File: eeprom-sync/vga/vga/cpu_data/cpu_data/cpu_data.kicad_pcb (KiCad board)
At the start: 2 copper layers, 78 x 44.7 mm, 34 parts, among them J1 Conn_02x06_Odd_Even, J10 Conn_01x03_Female, J11 Conn_01x02_Female, J12 Conn_02x05_Odd_Even, J2 Conn_01x04_Male, J3 Conn_01x04_Female, J4 Conn_01x15_Female, J5 Conn_01x15_Female, J6 Conn_01x08_Female, J7 Conn_02x03_Odd_Even, J8 Conn_02x08_Odd_Even, J9 Conn_01x08_Female, Q1 Q_NMOS_GSD, U1 GAL22V10, U2 74HC14, U3 74LS02, U4 IDT7205L12JG, U5 74LS573

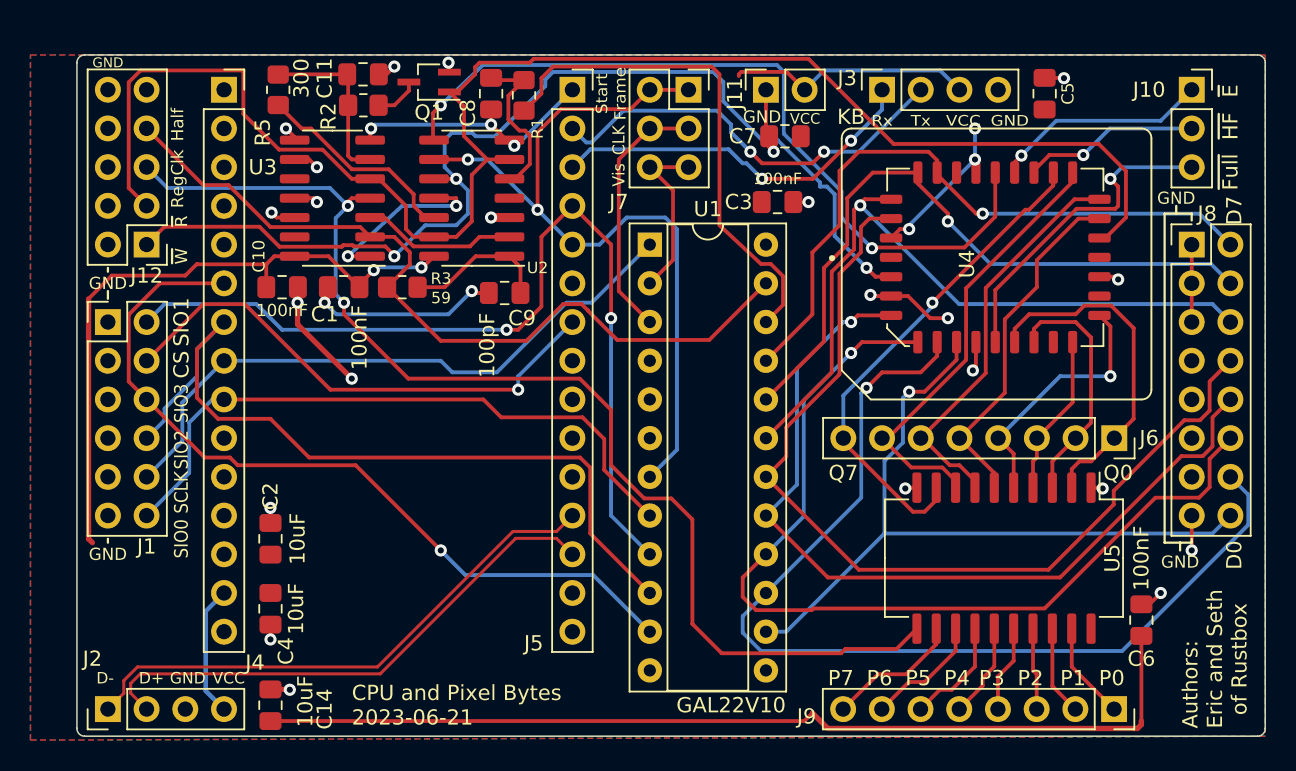
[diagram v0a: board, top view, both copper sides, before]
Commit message: added power and pixel indicator LEDs, rearranged and changed some headers for clearance of the GAL, fixed a location issue with a decoup cap
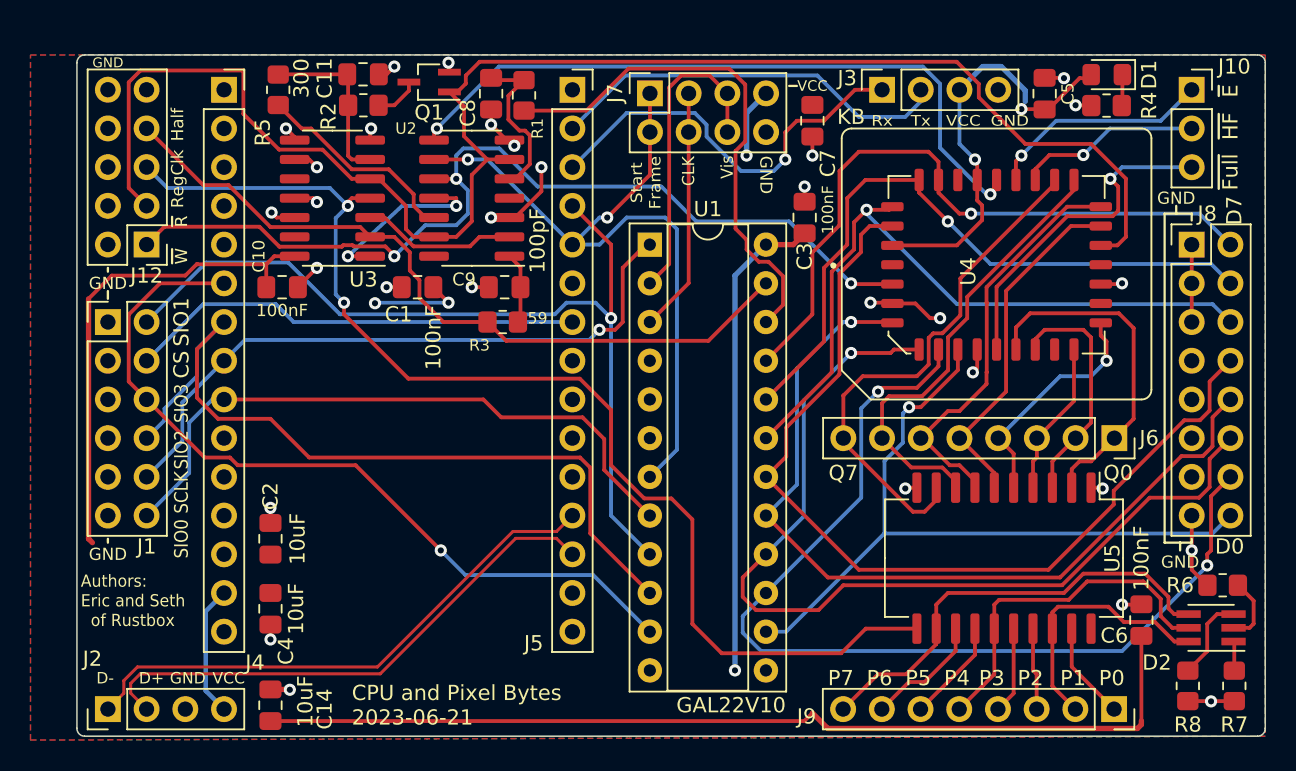
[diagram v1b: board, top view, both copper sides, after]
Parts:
- removed J11: Conn_01x02_Female, Connector_PinSocket_2.54mm:PinSocket_1x02_P2.54mm_Vertical
- added D1: LED, LED_SMD:LED_0805_2012Metric_Pad1.15x1.40mm_HandSolder, F.Cu at (146.8, 60.0)
- added D2: LED_RGB, LED_SMD:LED_Avago_PLCC6_3x2.8mm, F.Cu at (153.7, 96.3)
- added R4: R, Resistor_SMD:R_0805_2012Metric_Pad1.20x1.40mm_HandSolder, F.Cu at (146.8, 62.0)
- added R6: R, Resistor_SMD:R_0805_2012Metric_Pad1.20x1.40mm_HandSolder, F.Cu at (154.4, 93.5)
- added R7: R, Resistor_SMD:R_0805_2012Metric_Pad1.20x1.40mm_HandSolder, F.Cu at (155.2, 100.1)
- added R8: R, Resistor_SMD:R_0805_2012Metric_Pad1.20x1.40mm_HandSolder, F.Cu at (152.1, 100.1)
- J7: value Conn_02x03_Odd_Even -> Conn_02x04_Odd_Even; footprint Connector_PinSocket_2.54mm:PinSocket_2x03_P2.54mm_Vertical -> Connector_PinSocket_2.54mm:PinSocket_2x04_P2.54mm_Vertical
- R1: value R -> 34
- moved R3 6.97 mm to (107.2, 76.2)
- moved C1 4.85 mm to (101.6, 73.9)
- moved J7 2.54 mm to (116.8, 61.2), turned to 90 degrees
- moved C7 2.07 mm to (127.5, 63.0), turned to -90 degrees
- moved C3 2.05 mm to (127.0, 69.3), turned to -90 degrees
- moved C9 0.38 mm to (107.3, 73.9)
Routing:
- net VCC: track 142.5 -> 174.5 mm, vias 5 -> 6
- net GND: track 75.8 -> 53.1 mm, vias 28 -> 30
- net /P7: track 8.90 -> 29.4 mm
- net /P4: track 6.23 -> 23.1 mm
- net /P1: track 5.91 -> 17.0 mm
- net /Vis: track 11.4 -> 20.5 mm
- net /~{W}: track 70.2 -> 61.7 mm
- net /Reset: track 52.1 -> 45.9 mm
- net Net-(D2-Pad3): track 0.00 -> 5.59 mm
- net Net-(C9-Pad1): track 9.58 -> 4.68 mm
- net Net-(R6-Pad1): track 0.00 -> 4.39 mm
- net /CS: track 34.2 -> 30.0 mm, vias 1 -> 0
- net /Half: track 53.4 -> 49.4 mm
- net /StartFrame: track 52.4 -> 48.6 mm
- net /KB_{Rx}: track 24.8 -> 27.1 mm, vias 2 -> 1
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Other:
- board text added: "J7"

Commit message: gnd-ing the /OE on the gal
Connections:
- U1 pad 13: unconnected-(U1-Pad13) -> GND

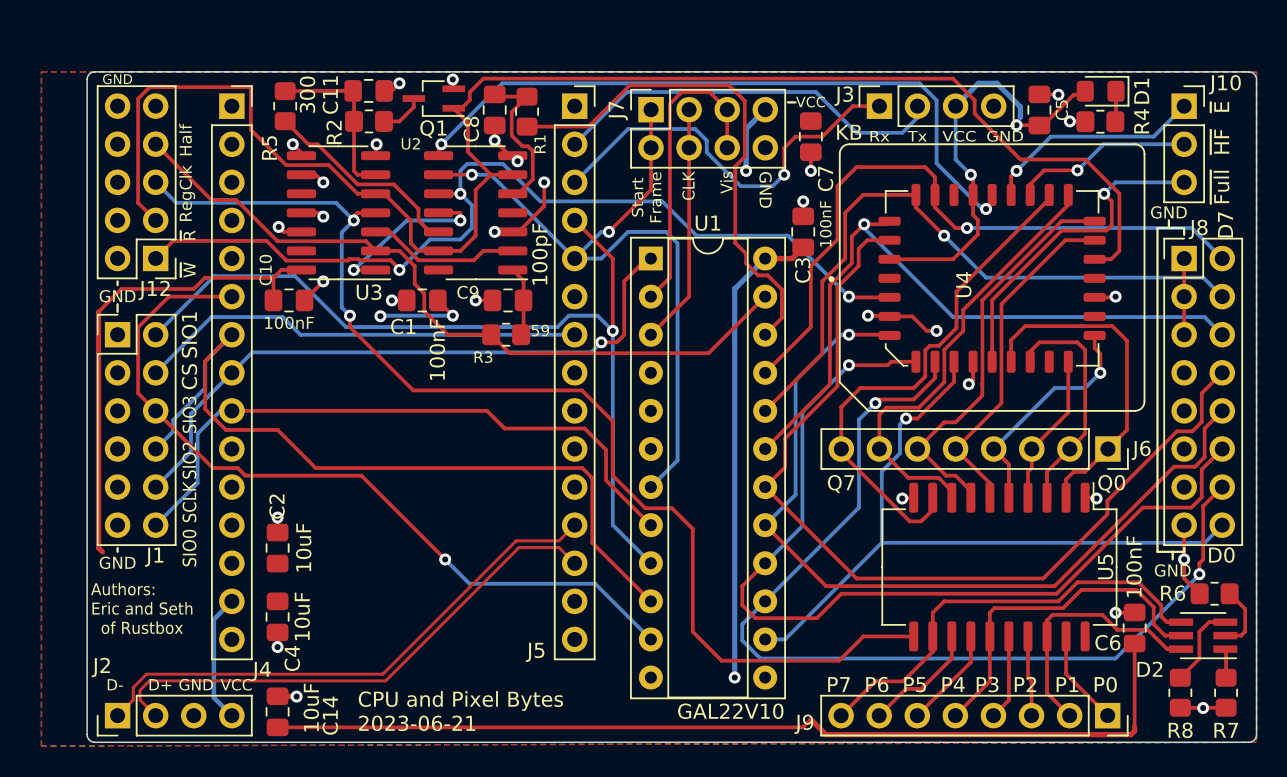
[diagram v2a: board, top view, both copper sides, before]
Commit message: updating board to use clocked latches as the data mile markers instead of RC time circuits. Also adding a clock board breadboardable circuit module
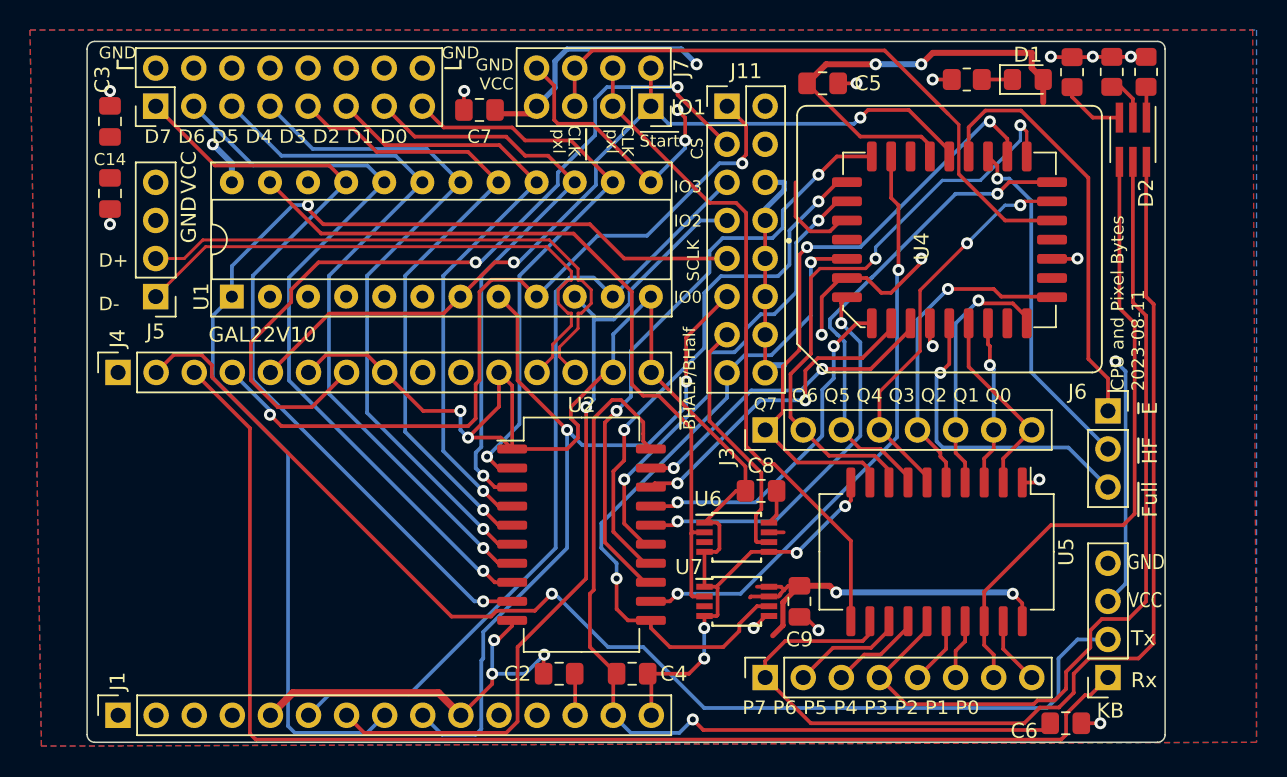
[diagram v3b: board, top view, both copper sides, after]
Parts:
- removed C1, C10: 100nF, Capacitor_SMD:C_0805_2012Metric_Pad1.18x1.45mm_HandSolder
- removed C11: 100pF, Capacitor_SMD:C_0805_2012Metric_Pad1.18x1.45mm_HandSolder
- removed J12: Conn_02x05_Odd_Even, Connector_PinHeader_2.54mm:PinHeader_2x05_P2.54mm_Vertical
- removed J9: Conn_01x08_Female, Connector_PinSocket_2.54mm:PinSocket_1x08_P2.54mm_Vertical
- removed Q1: Q_NMOS_GSD, Package_TO_SOT_SMD:SOT-323_SC-70_Handsoldering
- removed R1: 34, Resistor_SMD:R_0805_2012Metric_Pad1.20x1.40mm_HandSolder
- removed R2: 50, Resistor_SMD:R_0805_2012Metric_Pad1.20x1.40mm_HandSolder
- removed R3: 59, Resistor_SMD:R_0805_2012Metric_Pad1.20x1.40mm_HandSolder
- removed R5: 300, Resistor_SMD:R_0805_2012Metric_Pad1.20x1.40mm_HandSolder
- removed U3: 74LS02, Package_SO:SOIC-14_3.9x8.7mm_P1.27mm
- added J11: Conn_02x08_Odd_Even, Connector_PinHeader_2.54mm:PinHeader_2x08_P2.54mm_Vertical, F.Cu at (121.9, 61.0)
- added U6: 74AUC2G125, Package_SO:TSSOP-8_3x3mm_P0.65mm, F.Cu at (122.6, 89.7)
- added U7: 74LVC2G240, Package_SO:TSSOP-8_3x3mm_P0.65mm, F.Cu at (122.6, 94.0)
- C8, C9: value 100pF -> 100nF
- J1: value Conn_02x06_Odd_Even -> Conn_01x15_Socket; footprint Connector_PinHeader_2.54mm:PinHeader_2x06_P2.54mm_Vertical -> Connector_PinSocket_2.54mm:PinSocket_1x15_P2.54mm_Vertical
- J10: value Conn_01x03_Female -> Conn_01x08_Socket; footprint Connector_PinSocket_2.54mm:PinSocket_1x03_P2.54mm_Vertical -> Connector_PinSocket_2.54mm:PinSocket_1x08_P2.54mm_Vertical
- J2: value Conn_01x04_Male -> Conn_01x04_Socket; footprint Connector_PinHeader_2.54mm:PinHeader_1x04_P2.54mm_Vertical -> Connector_PinSocket_2.54mm:PinSocket_1x04_P2.54mm_Vertical
- J3: value Conn_01x04_Female -> Conn_01x08_Socket; footprint Connector_PinSocket_2.54mm:PinSocket_1x04_P2.54mm_Vertical -> Connector_PinHeader_2.54mm:PinHeader_1x08_P2.54mm_Vertical
- J4: value Conn_01x15_Female -> Conn_01x15_Socket
- J5: value Conn_01x15_Female -> Conn_01x04_Pin; footprint Connector_PinSocket_2.54mm:PinSocket_1x15_P2.54mm_Vertical -> Connector_PinHeader_2.54mm:PinHeader_1x04_P2.54mm_Vertical
- J6: value Conn_01x08_Female -> Conn_01x03_Socket; footprint Connector_PinSocket_2.54mm:PinSocket_1x08_P2.54mm_Vertical -> Connector_PinSocket_2.54mm:PinSocket_1x03_P2.54mm_Vertical
- U2: value 74HC14 -> 74LS573; footprint Package_SO:SOIC-14_3.9x8.7mm_P1.27mm -> Package_SO:SOIC-20W_7.5x15.4mm_P1.27mm
- moved J8 69.3 mm to (83.8, 61.0), turned to 90 degrees
- moved J2 66.1 mm to (147.3, 99.1), turned to 180 degrees
- moved J10 47.2 mm to (124.5, 99.1), turned to 90 degrees
- moved C3 46.8 mm to (80.8, 62.0)
- moved R7 42.6 mm to (144.9, 58.7), turned to 90 degrees
- moved R8 41.5 mm to (149.9, 58.7), turned to 90 degrees
- moved C14 36.3 mm to (80.8, 66.8), turned to 90 degrees
- moved R6 35.5 mm to (147.6, 58.7), turned to 90 degrees
- moved D2 33.4 mm to (149.0, 63.2), turned to -90 degrees
- moved C8 31.0 mm to (124.2, 86.6), turned to 0 degrees
- moved J5 30.7 mm to (83.8, 73.7), turned to 180 degrees
- moved U1 28.1 mm to (88.9, 73.7), turned to 90 degrees
- moved C9 27.9 mm to (126.7, 94.0), turned to 90 degrees
- moved J1 25.4 mm to (81.3, 101.6), turned to 90 degrees
- moved C4 23.9 mm to (115.6, 98.8), turned to 180 degrees
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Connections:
- C8 pad 1: Net-(C8-Pad1) -> GND
- C8 pad 2: GND -> VCC
- C9 pad 1: Net-(C9-Pad1) -> GND
- C9 pad 2: GND -> VCC
- D2 pad 1: Net-(D2-Pad1) -> Net-(D2-RK)
- D2 pad 3: Net-(D2-Pad3) -> Net-(D2-BK)
- D2 pad 4: /P7 -> /P1
- D2 pad 6: /P1 -> /P7
- J1 pad 10: /SCLK -> GND
- J1 pad 11: GND -> unconnected-(J1-Pin_11-Pad11)
- J1 pad 12: /SIO0 -> unconnected-(J1-Pin_12-Pad12)
- J1 pad 2: /SIO1 -> unconnected-(J1-Pin_2-Pad2)
- J1 pad 3: GND -> unconnected-(J1-Pin_3-Pad3)
- J1 pad 4: /CS -> unconnected-(J1-Pin_4-Pad4)
- J1 pad 7: GND -> /SIO2
- J1 pad 8: /SIO2 -> /SCLK
- J1 pad 9: GND -> /SIO0
- J10 pad 1: /Empty -> /P7
- J10 pad 2: /HalfFull -> /P6
- J10 pad 3: /Full -> /P5
- J2 pad 1: /D- -> /KB_{Rx}
- J2 pad 2: /D+ -> /KB_{Tx}
- J2 pad 3: GND -> VCC
- J2 pad 4: VCC -> GND
- J3 pad 1: /KB_{Rx} -> /Q7
- J3 pad 2: /KB_{Tx} -> /Q6
- J3 pad 3: VCC -> /Q5
- J3 pad 4: GND -> /Q4
- J4 pad 10: GND -> unconnected-(J4-Pin_10-Pad10)
- J4 pad 11: unconnected-(J4-Pad11) -> GND
- J4 pad 12: unconnected-(J4-Pad12) -> /D-
- J4 pad 13: VCC -> /D+
- J4 pad 14: VCC -> GND
- J4 pad 2: unconnected-(J4-Pad2) -> /KB_{Tx}
- J4 pad 3: unconnected-(J4-Pad3) -> /KB_{Rx}
- J4 pad 4: unconnected-(J4-Pad4) -> /SIO1
- J4 pad 5: GND -> /~{StartFrame}
- J4 pad 6: /SIO3 -> GND
- J4 pad 7: /SIO2 -> /CS
- J4 pad 8: /SCLK -> GND
- J4 pad 9: /SIO0 -> unconnected-(J4-Pin_9-Pad9)
- J5 pad 1: GND -> /D-
- J5 pad 2: /KB_{Tx} -> /D+
- J5 pad 3: /KB_{Rx} -> GND
- J5 pad 4: /SIO1 -> VCC
- J6 pad 1: /Q0 -> /Empty
- J6 pad 2: /Q1 -> /HalfFull
- J6 pad 3: /Q2 -> /Full
- J7 pad 1: /StartFrame -> /~{StartFrame}
- J7 pad 2: /StartFrame -> /~{StartFrame}
- J7 pad 3: /CLK -> /CLK_{pixel}
- J7 pad 4: /CLK -> /CLK_{pixel}
- J7 pad 5: /Vis -> /~{CLK_{pixel}}
- J7 pad 6: /Vis -> /~{CLK_{pixel}}
- J8 pad 1: GND -> /D7
- J8 pad 10: /D3 -> GND
- J8 pad 11: GND -> /D2
- J8 pad 12: /D2 -> GND
- J8 pad 13: GND -> /D1
- J8 pad 14: /D1 -> GND
- J8 pad 15: GND -> /D0
- J8 pad 16: /D0 -> GND
- J8 pad 2: /D7 -> GND
- J8 pad 3: GND -> /D6
- J8 pad 4: /D6 -> GND
- J8 pad 5: GND -> /D5
- J8 pad 6: /D5 -> GND
- J8 pad 7: GND -> /D4
- J8 pad 8: /D4 -> GND
- J8 pad 9: GND -> /D3
- R7 pad 1: Net-(D2-Pad1) -> Net-(D2-BK)
- R8 pad 1: Net-(D2-Pad3) -> Net-(D2-RK)
- U1 pad 2: /Vis -> unconnected-(U1-I2-Pad2)
- U1 pad 22: /CLK_{pixel} -> unconnected-(U1-IO2-Pad22)
- U1 pad 3: /CLK -> unconnected-(U1-I3-Pad3)
- U1 pad 7: /StartFrame -> /~{StartFrame}
- U2 pad 1: Net-(C9-Pad1) -> GND
- U2 pad 10: /~{W} -> GND
- U2 pad 11: Net-(U2-Pad11) -> /~{BHalf}
- U2 pad 12: Net-(R5-Pad2) -> /L7
- U2 pad 13: /~{R} -> /L6
- U2 pad 14: VCC -> /L5
- U2 pad 2: Net-(U2-Pad2) -> /D0
- U2 pad 3: GND -> /D1
- U2 pad 4: unconnected-(U2-Pad4) -> /D2
- U2 pad 5: Net-(C8-Pad1) -> /D3
- U2 pad 6: /~{R} -> /D4
- U2 pad 7: GND -> /D5
- U2 pad 8: /Reset -> /D6
- U2 pad 9: /StartFrame -> /D7
- U4 pad 18: /~{R} -> /~{CLK_{pixel}}
- U4 pad 2: /~{W} -> /~{BHalf}
- U4 pad 25: /Reset -> /~{StartFrame}
- U4 pad 28: /D7 -> /L7
- U4 pad 29: /D6 -> /L6
- U4 pad 30: /D5 -> /L5
- U4 pad 31: /D4 -> /L4
- U4 pad 4: /D3 -> /L3
- U4 pad 5: /D2 -> /L2
- U4 pad 6: /D1 -> /L1
- U4 pad 7: /D0 -> /L0
- U5 pad 11: /RegClk -> /CLK_{pixel}
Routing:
- net GND: track 53.1 -> 189.6 mm, vias 30 -> 27
- net /~{R}: track 105.3 -> 0.00 mm
- net /RegClk: track 77.4 -> 0.00 mm, vias 2 -> 0
- net /~{W}: track 61.7 -> 0.00 mm, vias 3 -> 0
- net /~{StartFrame}: track 0.00 -> 58.5 mm, vias 0 -> 2
- net /KB_{Rx}: track 27.1 -> 85.5 mm, vias 1 -> 0
- net /KB_{Tx}: track 26.6 -> 78.8 mm, vias 0 -> 1
- net /StartFrame: track 48.6 -> 0.00 mm, vias 2 -> 0
- net /Reset: track 45.9 -> 0.00 mm, vias 2 -> 0
- net /~{BHalf}: track 0.00 -> 45.8 mm, vias 0 -> 2
- net /P7: track 29.4 -> 72.1 mm
- net /~{CLK_{pixel}}: track 0.00 -> 41.5 mm
- net /L6: track 0.00 -> 40.6 mm, vias 0 -> 2
- net /L7: track 0.00 -> 39.9 mm, vias 0 -> 2
- net /L5: track 0.00 -> 35.6 mm, vias 0 -> 2
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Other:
- board size 78 x 44.7 mm -> 71.9 x 46.7 mm
- board text added: "CPU and Pixel Bytes 2023-08-11"
- board text added: "D+ D-"
- board text added: "D0 D1 D2 D3 D4 D5 D6 D7"
- board text added: "D7 D6 D5 D4 D3 D2 D1 D0"
- board text added: "GND VCC Tx Rx"
- board text added: "IO0"
- board text added: "IO1"
- board text added: "IO2"
- board text added: "IO3"
- board text added: "P0 P1 P2 P3 P4 P5 P6 P7"
- board text added: "P7 P6 P5 P4 P3 P2 P1 P0"
- board text added: "Q0 Q1 Q2 Q3 Q4 Q5 Q6"
- board text added: "Q6 Q5 Q4 Q3 Q2 Q1 Q0"
- board text added: "pxl"
- board text added: "~{BHALF}/BHalf"
- board text added: "~{Start}"
- board text removed: "CPU and Pixel Bytes 2023-06-21"
- board text removed: "D0"
- board text removed: "D7"
- board text removed: "Half"
- board text removed: "J1"
- board text removed: "J10"
- board text removed: "J12"
- board text removed: "J2"
- board text removed: "J3"
- board text removed: "J4"
- board text removed: "J5"
- board text removed: "J6"
- board text removed: "J7"
- board text removed: "J8"
- board text removed: "J9"
- board text removed: "P0"
- board text removed: "P1"
- board text removed: "P2"
- board text removed: "P3"
- board text removed: "P4"
- board text removed: "P5"
- board text removed: "P6"
- board text removed: "P7"
- board text removed: "Q0"
- board text removed: "RegClk"
- board text removed: "SIO0"
- board text removed: "SIO1"
- board text removed: "SIO2"
- board text removed: "SIO3"
- board text removed: "Start Frame"
- board text removed: "U1"
- board text removed: "Vis"
- board text removed: "~{R}"
- board text removed: "~{W}"

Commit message: final board
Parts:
- removed C8, C9: 100nF, Capacitor_SMD:C_0805_2012Metric_Pad1.18x1.45mm_HandSolder
- removed J11: Conn_02x08_Odd_Even, Connector_PinHeader_2.54mm:PinHeader_2x08_P2.54mm_Vertical
- removed U5: 74LS573, Package_SO:SOIC-20W_7.5x15.4mm_P1.27mm
- removed U6: 74AUC2G125, Package_SO:TSSOP-8_3x3mm_P0.65mm
- removed U7: 74LVC2G240, Package_SO:TSSOP-8_3x3mm_P0.65mm
- added C10: 100nF, Capacitor_SMD:C_0805_2012Metric_Pad1.18x1.45mm_HandSolder, F.Cu at (-77.2, 159.0)
- added J9: Conn_02x07_Odd_Even, Connector_PinHeader_2.54mm:PinHeader_2x07_P2.54mm_Vertical, F.Cu at (-99.1, 144.8)
- added U3: 74AHCT244, Package_SO:TSSOP-20_4.4x6.5mm_P0.65mm, F.Cu at (-79.5, 153.4)
- U2: value 74LS573 -> 74HCT574; footprint Package_SO:SOIC-20W_7.5x15.4mm_P1.27mm -> Package_SO:SOIC-20W_7.5x12.8mm_P1.27mm
- moved D1 250.2 mm to (-99.1, 126.2)
- moved R4 249.3 mm to (-102.4, 125.7), turned to -90 degrees
- moved J7 220.9 mm to (-94.0, 127.0), turned to 90 degrees
- moved J2 220.2 mm to (-71.1, 127.0), turned to -90 degrees
- moved R8 215.2 mm to (-44.5, 151.1), turned to 0 degrees
- moved R6 214.2 mm to (-44.5, 153.7), turned to 0 degrees
- moved C5 212.8 mm to (-70.6, 135.1), turned to 0 degrees
- moved C6 211.5 mm to (-61.5, 150.4), turned to 0 degrees
- moved R7 209.9 mm to (-44.5, 149.1), turned to 0 degrees
- moved D2 209.0 mm to (-45.6, 139.7), turned to 90 degrees
- moved J8 205.6 mm to (-101.6, 149.9), turned to 0 degrees
- moved U4 205.0 mm to (-58.1, 133.5)
- moved C7 200.5 mm to (-83.3, 128.8), turned to -90 degrees
- moved J6 199.6 mm to (-45.7, 132.1), turned to 180 degrees
- moved U1 194.4 mm to (-94.0, 139.7), turned to 0 degrees
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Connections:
- J7 pad 3: /CLK_{pixel} -> /Clk
- J7 pad 4: /CLK_{pixel} -> /Clk
- J7 pad 5: /~{CLK_{pixel}} -> /Vis
- J7 pad 6: /~{CLK_{pixel}} -> /Vis
- U1 pad 2: unconnected-(U1-I2-Pad2) -> /Vis
- U1 pad 22: unconnected-(U1-IO2-Pad22) -> /Clk_{pixel}
- U1 pad 3: unconnected-(U1-I3-Pad3) -> /Clk
- U2 pad 11: /~{BHalf} -> /Clk_{pixel}
- U2 pad 12: /L7 -> /P7
- U2 pad 13: /L6 -> /P6
- U2 pad 14: /L5 -> /P5
- U2 pad 15: /L4 -> /P4
- U2 pad 16: /L3 -> /P3
- U2 pad 17: /L2 -> /P2
- U2 pad 18: /L1 -> /P1
- U2 pad 19: /L0 -> /P0
- U2 pad 2: /D0 -> /Q0
- U2 pad 3: /D1 -> /Q1
- U2 pad 4: /D2 -> /Q2
- U2 pad 5: /D3 -> /Q3
- U2 pad 6: /D4 -> /Q4
- U2 pad 7: /D5 -> /Q5
- U2 pad 8: /D6 -> /Q6
- U2 pad 9: /D7 -> /Q7
- U4 pad 18: /~{CLK_{pixel}} -> /Clk_{pixel}
- U4 pad 2: /~{BHalf} -> /Half
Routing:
- net VCC: track 163.4 -> 65.7 mm
- net /Clk_{pixel}: track 0.00 -> 88.3 mm, vias 0 -> 3
- net GND: track 189.6 -> 101.7 mm, vias 27 -> 28
- net /KB_{Rx}: track 85.5 -> 19.9 mm, vias 0 -> 1
- net /KB_{Tx}: track 78.8 -> 27.9 mm
- net /~{BHalf}: track 45.8 -> 0.00 mm, vias 2 -> 0
- net /CLK_{pixel}: track 44.9 -> 0.00 mm
- net /~{CLK_{pixel}}: track 41.5 -> 0.00 mm
- net /Q1: track 11.0 -> 51.3 mm, vias 1 -> 2
- net /Q0: track 13.1 -> 49.3 mm, vias 0 -> 2
- net /~{StartFrame}: track 58.5 -> 94.2 mm, vias 2 -> 1
- net /D7: track 54.0 -> 21.6 mm, vias 1 -> 0
- net /D6: track 51.1 -> 21.1 mm, vias 1 -> 0
- net /D5: track 48.4 -> 20.6 mm, vias 1 -> 0
- net /D4: track 46.1 -> 20.5 mm, vias 1 -> 0
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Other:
- board size 71.9 x 46.7 mm -> 66 x 46.7 mm
- board text added: "CPU and Pixel Bytes 2023-08-26"
- board text added: "D- D+"
- board text added: "Half"
- board text added: "Q0"
- board text added: "Q0 Q1 Q2 Q3 Q4 Q5 Q6 Q7"
- board text added: "~{CLK}"
- board text added: "~{Start} Clk Vis"
- board text removed: "CPU and Pixel Bytes 2023-08-11"
- board text removed: "D+ D-"
- board text removed: "J11"
- board text removed: "P0 P1 P2 P3 P4 P5 P6 P7"
- board text removed: "Q0 Q1 Q2 Q3 Q4 Q5 Q6"
- board text removed: "Q6 Q5 Q4 Q3 Q2 Q1 Q0"
- board text removed: "~{BHALF}/BHalf"
